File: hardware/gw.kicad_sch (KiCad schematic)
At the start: 21 parts, among them J1 USB_OTG, J2 Conn_01x04, U1 ESP-12F, U2 Ai-Thinker-Ra-02, U3 AMS1117-3.3

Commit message: Name changes
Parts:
- D1: value RF -> WIFI
- D2: value WIFI -> RF
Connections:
- net RF_LED: now also R4.1, R8.2, U1.12 (GPIO0); no longer R2.2, U1.4 (GPIO16)
- net WF_LED: now also R2.2, U1.4 (GPIO16); no longer R4.1, R8.2, U1.12 (GPIO0)
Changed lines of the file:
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@@
     (effects (font (size 1.27 1.27)) (justify right bottom))
   )
-  (label "RF_LED" (at 127.762 74.295 180)
+  (label "WF_LED" (at 127.762 74.295 180)
     (effects (font (size 1.27 1.27)) (justify right bottom))
   )
@@
     (effects (font (size 1.27 1.27)) (justify right bottom))
   )
-  (label "RF_LED" (at 24.765 38.862 0)
+  (label "RF_LED" (at 24.765 46.355 0)
     (effects (font (size 1.27 1.27)) (justify left bottom))
   )
@@
     (effects (font (size 1.27 1.27)) (justify right bottom))
   )
-  (label "WF_LED" (at 24.765 46.355 0)
-    (effects (font (size 1.27 1.27)) (justify left bottom))
-  )
-  (label "WF_LED" (at 127.635 48.895 180)
+  (label "WF_LED" (at 24.765 38.862 0)
+    (effects (font (size 1.27 1.27)) (justify left bottom))
+  )
+  (label "RF_LED" (at 127.635 48.895 180)
     (effects (font (size 1.27 1.27)) (justify right bottom))
   )
@@
       (effects (font (size 1 1)))
     )
-    (property "Value" "WIFI" (id 1) (at 41.021 49.149 0)
+    (property "Value" "RF" (id 1) (at 41.021 49.149 0)
       (effects (font (size 1 1)))
     )
@@
       (effects (font (size 1 1)))
     )
-    (property "Value" "RF" (id 1) (at 41.021 41.783 0)
+    (property "Value" "WIFI" (id 1) (at 41.021 41.783 0)
       (effects (font (size 1 1)))
     )
@@
     )
     (path "/c393e337-c86b-4e91-bda3-34dd1303e50d"
-      (reference "D1") (unit 1) (value "RF") (footprint "LED_SMD:LED_1206_3216Metric")
+      (reference "D1") (unit 1) (value "WIFI") (footprint "LED_SMD:LED_1206_3216Metric")
     )
     (path "/9225438f-945b-4a6c-98f4-260eed355a21"
-      (reference "D2") (unit 1) (value "WIFI") (footprint "LED_SMD:LED_1206_3216Metric")
+      (reference "D2") (unit 1) (value "RF") (footprint "LED_SMD:LED_1206_3216Metric")
     )
     (path "/8c86306e-96c4-4b0a-8947-81247a67493f"

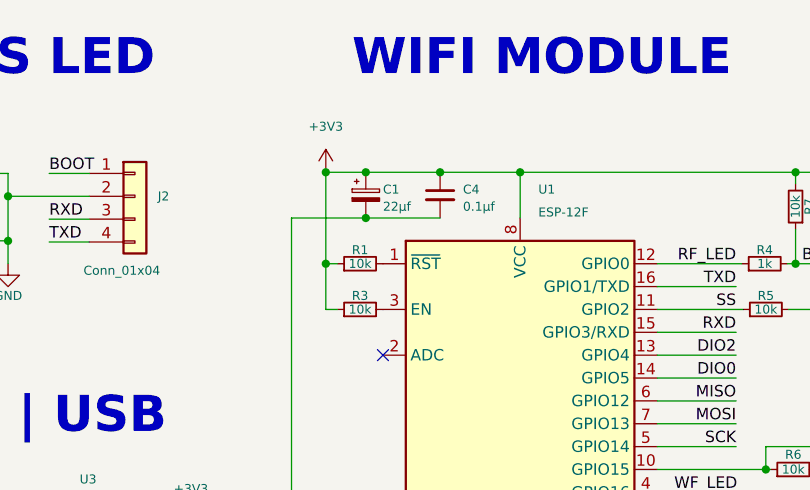
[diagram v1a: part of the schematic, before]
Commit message: Change resistor value
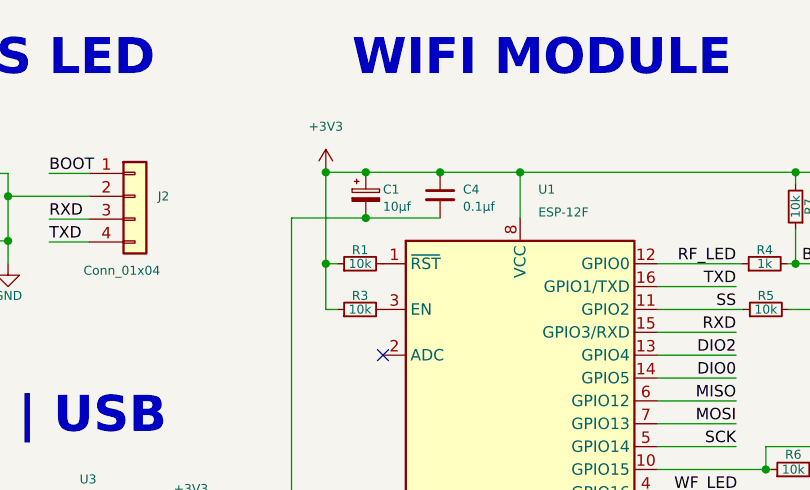
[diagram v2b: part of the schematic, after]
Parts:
- C1: value 22µf -> 10µf
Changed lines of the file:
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@@
       (effects (font (size 1 1)) (justify left))
     )
-    (property "Value" "22µf" (id 1) (at 88.392 42.545 0)
+    (property "Value" "10µf" (id 1) (at 88.392 42.545 0)
       (effects (font (size 1 1)) (justify left))
     )
@@
     )
     (path "/5723f912-a642-4b64-a661-21e0c8eeaa69"
-      (reference "C1") (unit 1) (value "22µf") (footprint "Capacitor_Tantalum_SMD:CP_EIA-3216-10_Kemet-I")
+      (reference "C1") (unit 1) (value "10µf") (footprint "Capacitor_Tantalum_SMD:CP_EIA-3216-10_Kemet-I")
     )
     (path "/54e331c4-c732-4227-b0b4-3a997ea83835"

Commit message: Fixes
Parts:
- removed R1, R5, R6, R7: 10k, Resistor_SMD:R_1206_3216Metric, symbol Device:R_Small
- added C7: 10µf, Capacitor_SMD:C_1206_3216Metric, symbol Device:C_Small
- C1: footprint Capacitor_Tantalum_SMD:CP_EIA-3216-10_Kemet-I -> Capacitor_SMD:C_1206_3216Metric; symbol Device:C_Polarized_Small -> Device:C_Small
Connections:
- net TXD is gone; now on net RF_LED: J2.4 (Pin_4), U1.16 (GPIO1/TXD)
- net +3V3: now also R3.2; no longer R3.1
- net GND: now also C7.2
- net RF_LED: no longer R4.1, U1.12 (GPIO0)
- net SS: now also U1.4 (GPIO16); no longer U1.11 (GPIO2)
- net WF_LED: now also R4.1, U1.12 (GPIO0); no longer U1.4 (GPIO16)
- net at U1.3 (EN): now also R3.1, C7.1; no longer R3.2
- no-connect marks 9 -> 11
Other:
- moved on the sheet: C4, C5, C6, R3, R4, U1, U2

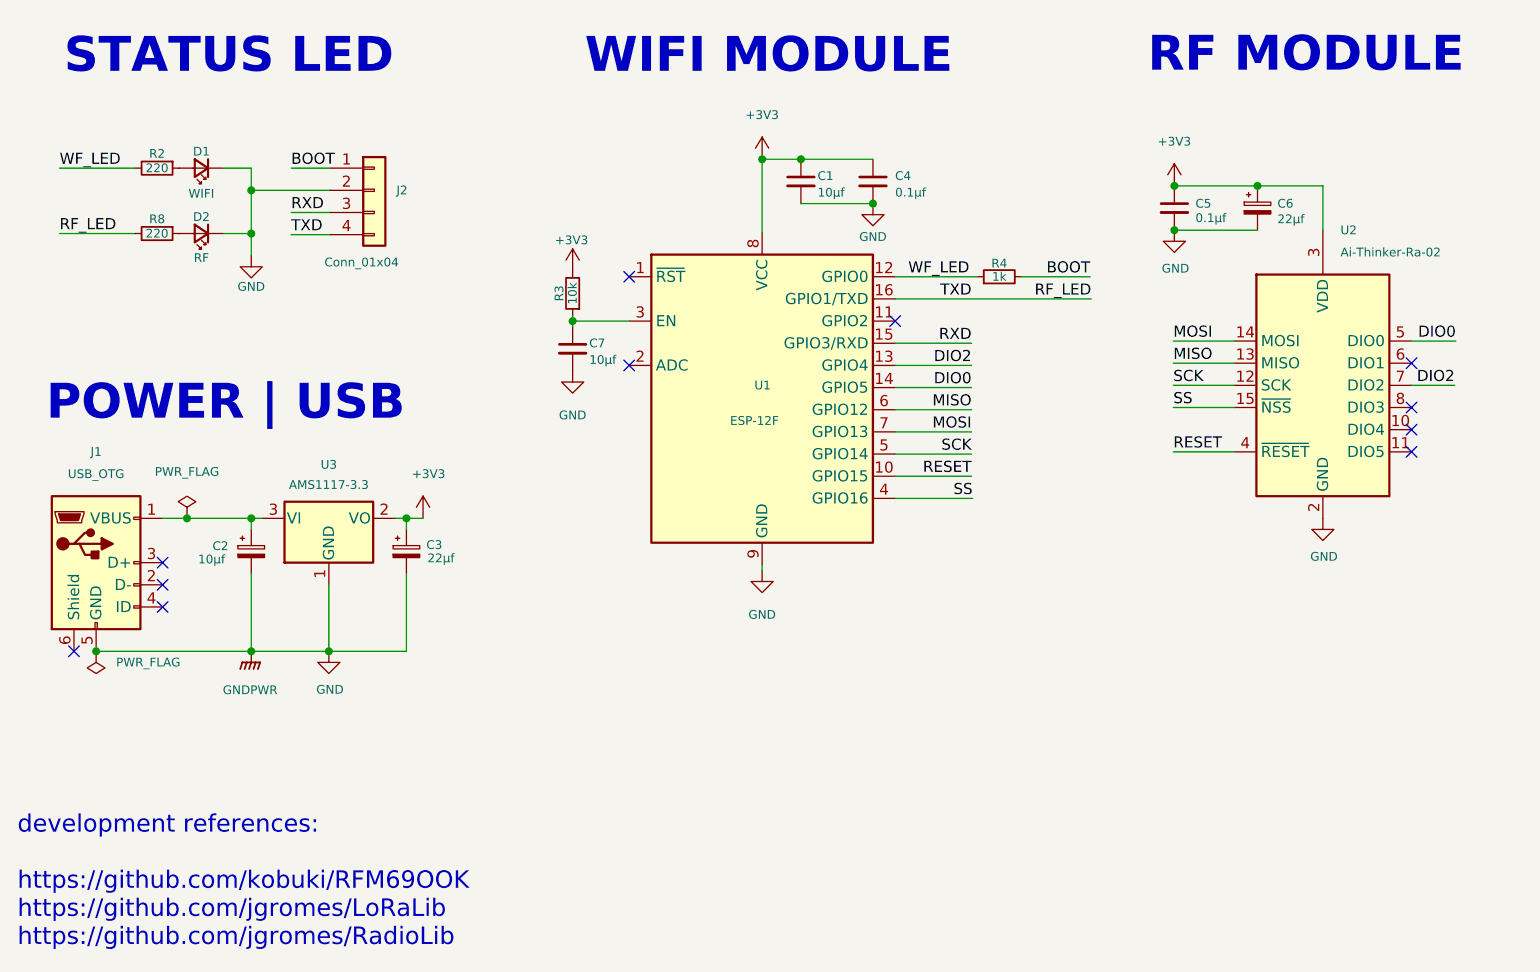
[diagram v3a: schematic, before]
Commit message: Revert "Fixes", move to ESP12F
This reverts commit ad443d04f57b2ab128a4687db847c72f3a41be2c.
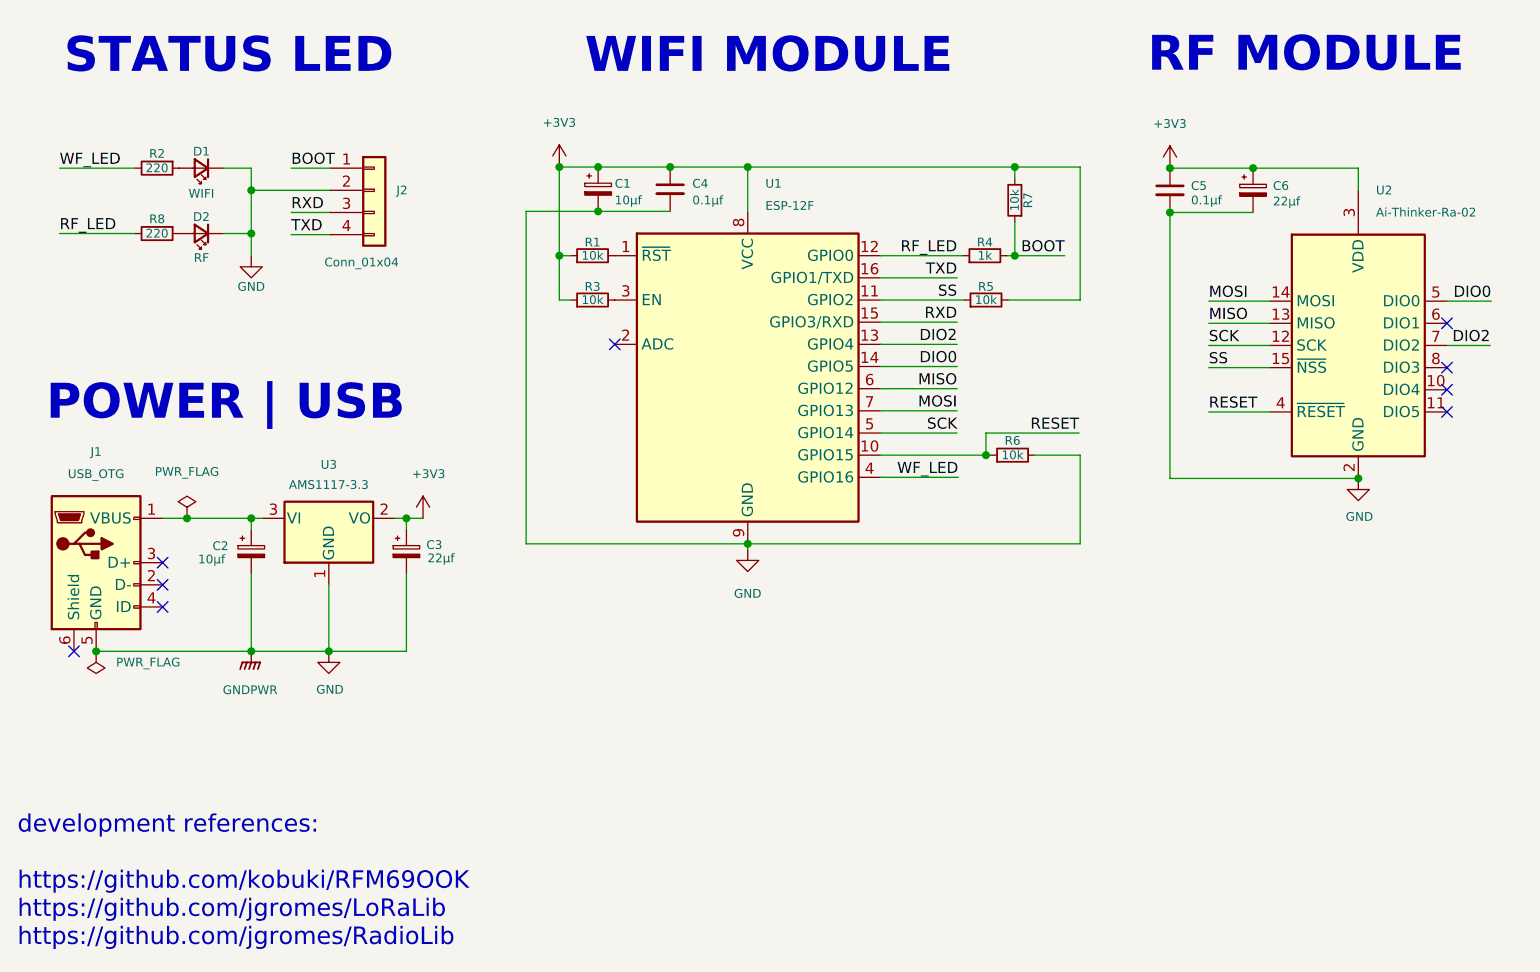
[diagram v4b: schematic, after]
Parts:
- removed C7: 10µf, Capacitor_SMD:C_1206_3216Metric, symbol Device:C_Small
- added R1, R5, R6, R7: 10k, Resistor_SMD:R_1206_3216Metric, symbol Device:R_Small
- C1: footprint Capacitor_SMD:C_1206_3216Metric -> Capacitor_Tantalum_SMD:CP_EIA-3216-10_Kemet-I; symbol Device:C_Small -> Device:C_Polarized_Small
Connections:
- net +3V3: now also R3.1, R1.1, R5.2, R7.2; no longer R3.2
- net BOOT: now also R7.1
- net GND: now also R6.2
- net RESET: now also R6.1
- net RF_LED: now also R4.1, U1.12 (GPIO0); no longer J2.4 (Pin_4), U1.16 (GPIO1/TXD)
- net SS: now also U1.11 (GPIO2), R5.1; no longer U1.4 (GPIO16)
- net WF_LED: now also U1.4 (GPIO16); no longer R4.1, U1.12 (GPIO0)
- net at U1.3 (EN): now also R3.2; no longer R3.1
- net at U1.1 (~{RST}): now also R1.2
- new net TXD: J2.4 (Pin_4), U1.16 (GPIO1/TXD)
- no-connect marks 11 -> 9
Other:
- moved on the sheet: C4, C5, C6, R3, R4, U1, U2

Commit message: Revert "Revert "Fixes", move to ESP12F", sticking to ESP12S now.
This reverts commit af2652227ade2a41ecb2737fc58930674a5f1724.
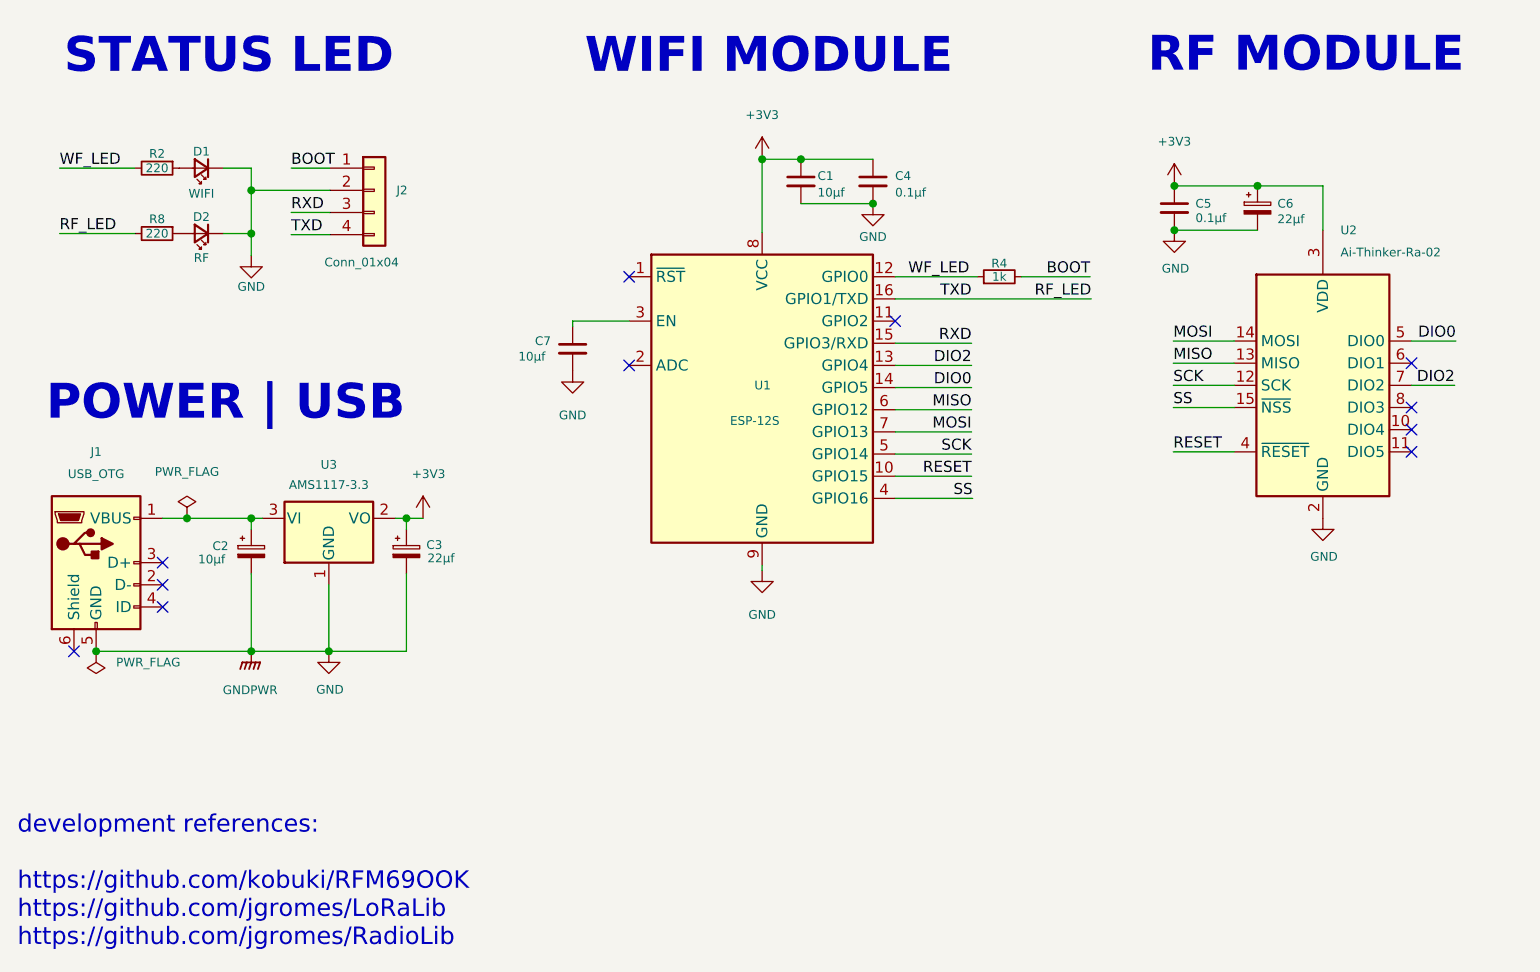
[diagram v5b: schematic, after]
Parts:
- removed R1, R3, R5, R6, R7: 10k, Resistor_SMD:R_1206_3216Metric, symbol Device:R_Small
- added C7: 10µf, Capacitor_SMD:C_1206_3216Metric, symbol Device:C_Small
- C1: footprint Capacitor_Tantalum_SMD:CP_EIA-3216-10_Kemet-I -> Capacitor_SMD:C_1206_3216Metric; symbol Device:C_Polarized_Small -> Device:C_Small
- U1: value ESP-12F -> ESP-12S
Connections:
- net TXD is gone; now on net RF_LED: J2.4 (Pin_4), U1.16 (GPIO1/TXD)
- net GND: now also C7.2
- net RF_LED: no longer R4.1, U1.12 (GPIO0)
- net SS: now also U1.4 (GPIO16); no longer U1.11 (GPIO2)
- net WF_LED: now also R4.1, U1.12 (GPIO0); no longer U1.4 (GPIO16)
- net at U1.3 (EN): now also C7.1
- no-connect marks 9 -> 11
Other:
- moved on the sheet: C4, C5, C6, R4, U1, U2

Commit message: Correct version in schematic
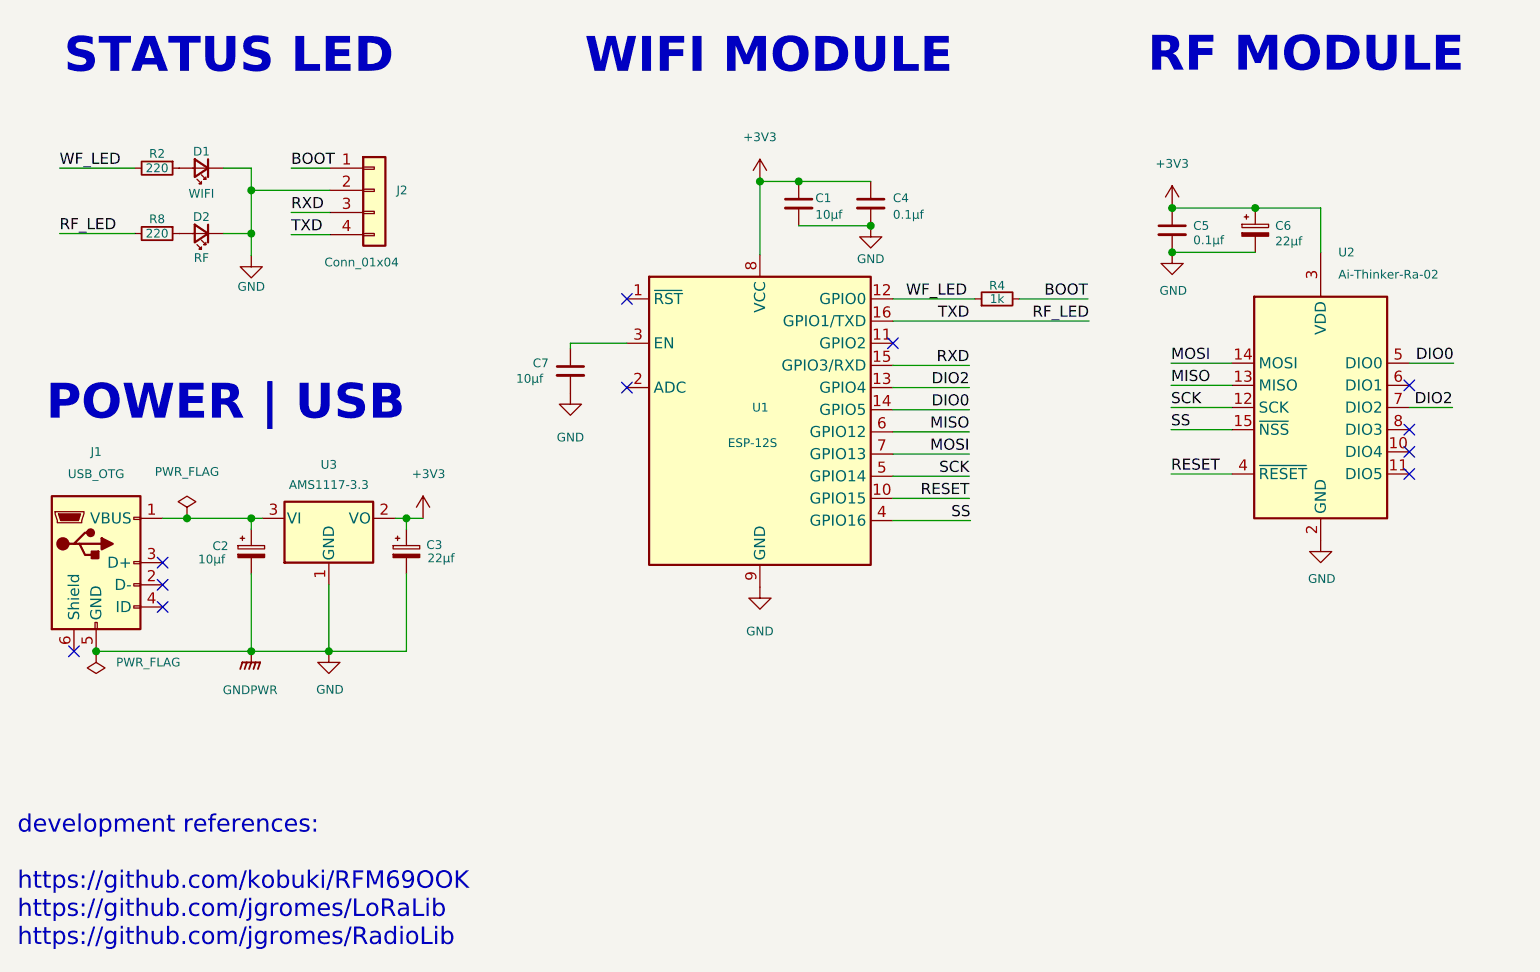
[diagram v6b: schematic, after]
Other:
- moved on the sheet: C1, C4, C5, C6, C7, R4, U1, U2
